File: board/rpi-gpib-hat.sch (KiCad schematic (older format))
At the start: 39 parts, among them J1 RPI_GPIO, J2 GPIB, U1 SN75160BDW, U2 SN75162BDW, U3 LM317_SOT-223, U4 CAT24C32

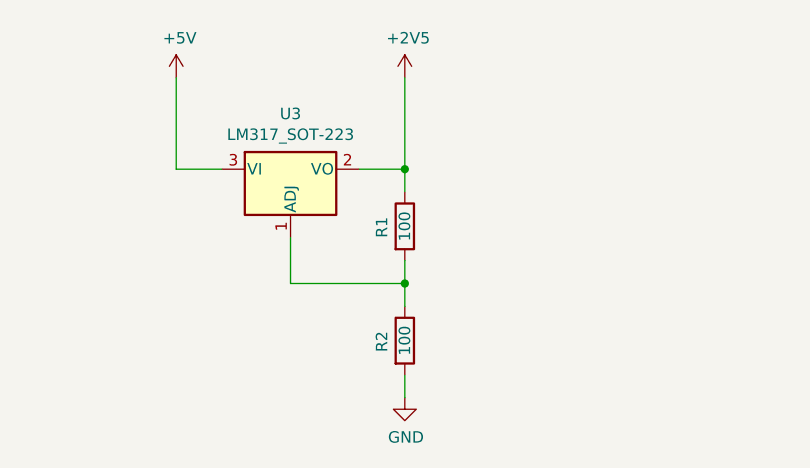
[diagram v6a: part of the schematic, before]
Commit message: Swap connectors to top of pico board.
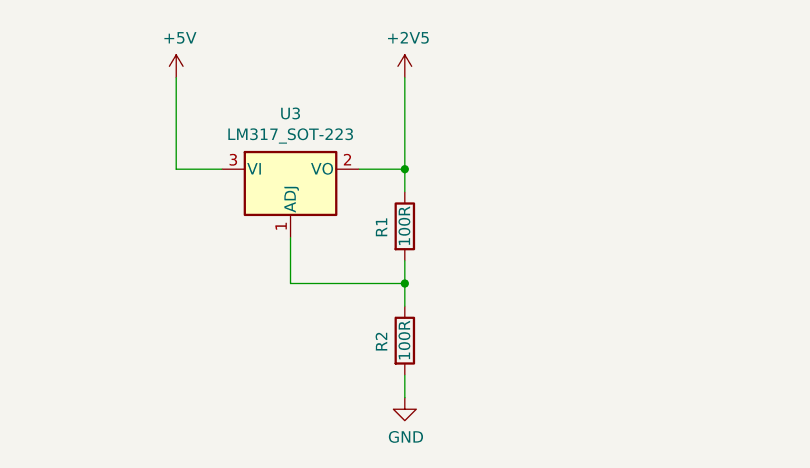
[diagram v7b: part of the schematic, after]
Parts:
- R1, R2: value 100 -> 100R
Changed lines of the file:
@@
 Title "Raspberry Pi GPIB µHAT"
 Date "2019-05-17"
-Rev "0.1"
-Comp "© 2019 Sam Hanes. Licensed under CERN OHL v1.2."
+Rev "0.2"
+Comp "© 2022 Sam Hanes. Licensed under CERN OHL v1.2."
 Comment1 "https://github.com/Elemecca/rpi-gpib"
 Comment2 ""
@@
 P 5500 6250
 F 0 "R1" V 5400 6200 50  0000 L CNN
-F 1 "100" V 5500 6250 50  0000 C CNN
+F 1 "100R" V 5500 6250 50  0000 C CNN
 F 2 "Resistor_SMD:R_0402_1005Metric" V 5430 6250 50  0001 C CNN
 F 3 "~" H 5500 6250 50  0001 C CNN
@@
 P 5500 6750
 F 0 "R2" V 5400 6700 50  0000 L CNN
-F 1 "100" V 5500 6750 50  0000 C CNN
+F 1 "100R" V 5500 6750 50  0000 C CNN
 F 2 "Resistor_SMD:R_0402_1005Metric" V 5430 6750 50  0001 C CNN
 F 3 "~" H 5500 6750 50  0001 C CNN
